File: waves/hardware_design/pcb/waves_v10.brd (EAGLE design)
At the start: 100 x 80 mm, 0 parts

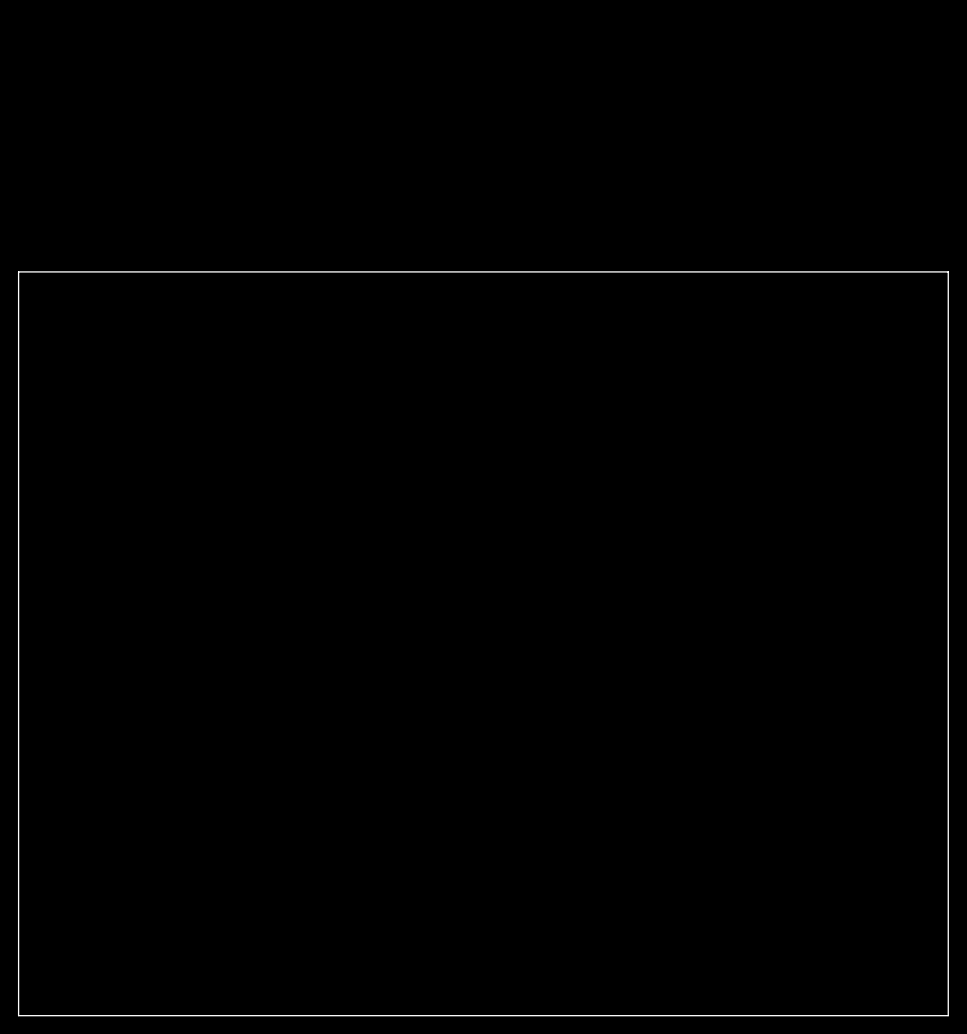
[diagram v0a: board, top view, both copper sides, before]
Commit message: added dac breakout and progress on schematic
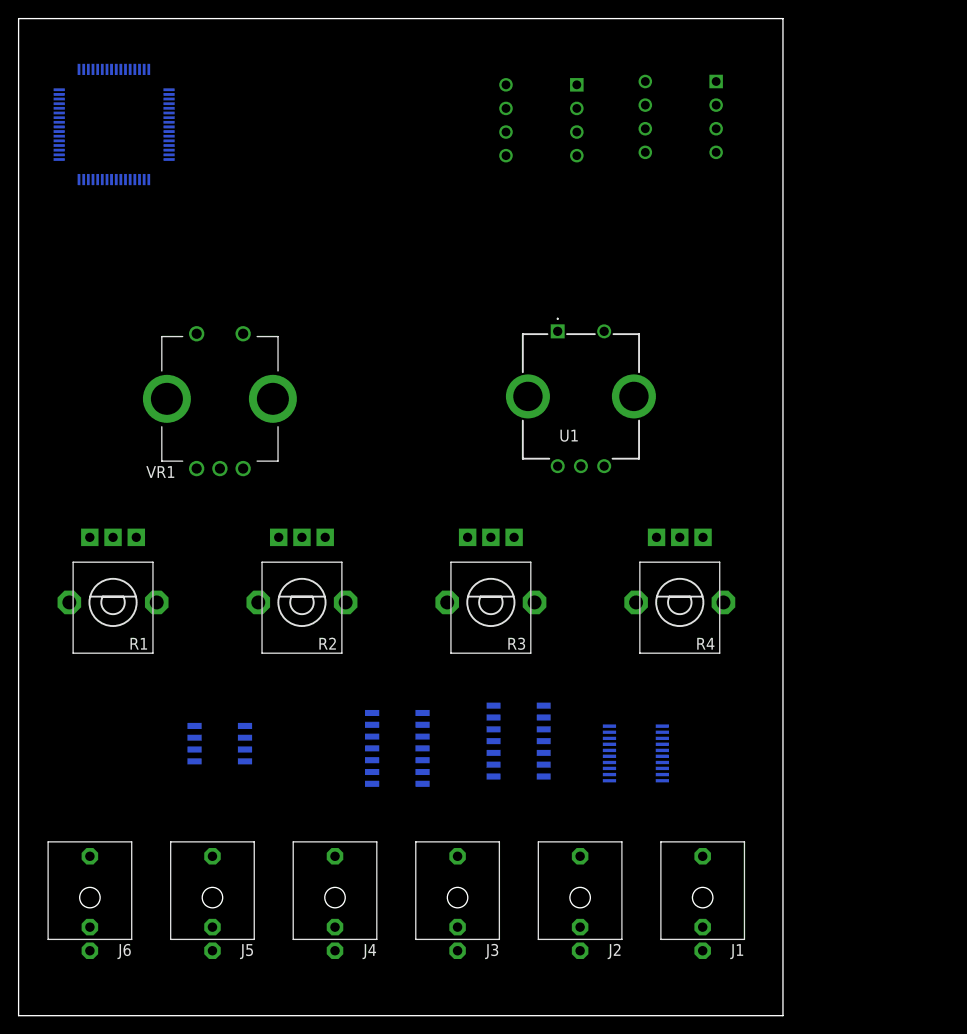
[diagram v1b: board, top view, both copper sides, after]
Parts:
- added IC1: PCM5100PW, og-dac:SSOP20
- added IC2: STM32F20X, marbles_v70:TQFP-10X10-64
- added IC3, IC4: 1-2199298-2, 1-2199298-2:DIPS762W70P254L1016H510Q8N
- added IC5: MCP6004T-I_SL, MCP6004T-I_SL:SOIC127P600X175-14N
- added IC6: TL074CD, TL074CD:SOIC127P600X175-14N
- added IC7: TL072CD, TL072CD:SOIC127P600X175-8N
- added J1, J2, J3, J4, J5, J6: PJ301_THONKICONN6, og-pj301:WQP_PJ_301M6
- added R1, R2, R3, R4: (no value), og-pots:ALPS_POT_VERTICAL_PS
- added U1: PEC11R-4215F-S0024, PEC11R-4215F-S0024:PEC11R4215FS0024
- added VR1: PEC11R-4220F-S0024, PEC11R-4220F-S0024:PEC11R4220FS0024
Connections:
- new net ENC_A: VR1.A1
- new net ENC_B: VR1.B1
- new net ENC_CLICK: VR1.2
- new net GND: VR1.1, VR1.C1
- new net VBAT: IC2.1
- new net VCAP_1: IC2.31
- new net VCAP_2: IC2.47
- new net VDDA: IC2.13
- new net VDD_1: IC2.32
- new net VDD_2: IC2.48
- new net VDD_3: IC2.64
- new net VDD_4: IC2.19
- new net VSSA: IC2.12
- new net VSS_3: IC2.63
- new net VSS_4: IC2.18
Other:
- board size 100 x 80 mm -> 82.2 x 107.2 mm
